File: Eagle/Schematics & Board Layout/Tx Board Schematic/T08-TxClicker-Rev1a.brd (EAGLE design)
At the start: 88.9 x 44.5 mm, 83 parts, among them U1 CC430F513X---RGZ48, X1-DNI SMA-SMD, Y1 26MHz

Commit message: layout update
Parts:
- added R17: (no value), QuadResistor:2012(4_RES)
- moved TP14 26.1 mm to (-18.5, 14.7)
- moved TP15 26.1 mm to (-18.5, 12.2)
- moved TP16 26.1 mm to (-18.5, 9.63)
- moved TP17 26.1 mm to (-18.5, 7.09)
- moved TP1 26.1 mm to (-20.4, 10.1)
- moved TP18 26.1 mm to (-16.0, 5.44)
- moved TP3 26.1 mm to (-23.0, 10.1)
- moved TP2 15.0 mm to (-12.7, 13.1)
- moved TP5 4.53 mm to (37.6, 22.7)
- moved C16 4.17 mm to (36.6, 7.72)
- moved C20 4.17 mm to (50.6, 2.13)
- moved C23 4.17 mm to (50.6, 4.67)
- moved C29 4.17 mm to (60.7, 9.88)
- moved C5 4.17 mm to (49.8, 24.6)
- moved C6 4.17 mm to (35.1, 24.7)
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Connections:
- new net N$19: R17.6, U1.2
- new net N$20: R17.8, U1.1
- new net N$7: R17.2, U1.4
- new net N$9: R17.4, U1.3
- net P1.7: now also R17.1; no longer U1.4
- net P2.0: now also R17.3; no longer U1.3
- net P2.1: now also R17.5; no longer U1.2
- net P2.2: now also R17.7; no longer U1.1
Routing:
- net P1.4: track 21.6 -> 41.3 mm, vias 2 -> 3
- net N$7: track 0.00 -> 7.17 mm
- net P2.1: track 19.6 -> 12.9 mm
- net P2.2: track 29.9 -> 24.1 mm
- net P1.7: track 44.2 -> 38.6 mm
- net N$9: track 0.00 -> 5.46 mm
- net N$15: track 45.9 -> 51.1 mm, vias 2 -> 0
- net RST/SBWTDIO: track 12.2 -> 8.19 mm
- net N$19: track 0.00 -> 3.80 mm
- net P2.0: track 30.9 -> 27.2 mm, vias 2 -> 0
- net P1.6/TX: track 19.9 -> 23.0 mm
- net N$20: track 0.00 -> 2.16 mm
- net P1.5/RX: track 21.7 -> 23.2 mm
- net VCC: track 155.7 -> 157.2 mm
- net TEST/SBWTCK: track 33.5 -> 34.0 mm, vias 2 -> 0
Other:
- board size 88.9 x 44.5 mm -> 84 x 41.7 mm

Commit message: layout update
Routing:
- net N$15: track 51.1 -> 46.9 mm, vias 0 -> 2
- net VCC: track 157.2 -> 158.4 mm
- net TEST/SBWTCK: track 34.0 -> 33.3 mm
- net P1.4: track 41.3 -> 41.4 mm, vias 3 -> 4

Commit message: Button Example
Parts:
- S1, S2, S3, S4: value TOUCHPAD_SWITCH_COMBO -> SWITCH-MOMENTARY-212MM
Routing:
- net P2.2: track 24.1 -> 29.4 mm
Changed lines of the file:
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@@
 <attribute name="OC_FARNELL" value="unknown" x="57.5564" y="18.0086" size="1.778" layer="27" display="off"/>
 </element>
-<element name="S1" library="SparkFun-Electromechanical--edited" package="TACTILE-PTH-12MM" value="TOUCHPAD_SWITCH_COMBO" x="46.6344" y="33.5026" rot="R270"/>
-<element name="S2" library="SparkFun-Electromechanical--edited" package="TACTILE-PTH-12MM" value="TOUCHPAD_SWITCH_COMBO" x="33.2994" y="33.6296" rot="R270"/>
-<element name="S3" library="SparkFun-Electromechanical--edited" package="TACTILE-PTH-12MM" value="TOUCHPAD_SWITCH_COMBO" x="20.2184" y="33.6296" rot="R270"/>
-<element name="S4" library="SparkFun-Electromechanical--edited" package="TACTILE-PTH-12MM" value="TOUCHPAD_SWITCH_COMBO" x="7.0104" y="33.6296" rot="R270"/>
+<element name="S1" library="SparkFun-Electromechanical--edited" package="TACTILE-PTH-12MM" value="SWITCH-MOMENTARY-212MM" x="46.6344" y="33.5026" rot="R270">
+<attribute name="PROD_ID" value="SWCH-09185" x="46.6344" y="33.5026" size="1.778" layer="27" rot="R270" display="off"/>
+</element>
+<element name="S2" library="SparkFun-Electromechanical--edited" package="TACTILE-PTH-12MM" value="SWITCH-MOMENTARY-212MM" x="33.2994" y="33.6296" rot="R270">
+<attribute name="PROD_ID" value="SWCH-09185" x="33.2994" y="33.6296" size="1.778" layer="27" rot="R270" display="off"/>
+</element>
+<element name="S3" library="SparkFun-Electromechanical--edited" package="TACTILE-PTH-12MM" value="SWITCH-MOMENTARY-212MM" x="20.2184" y="33.6296" rot="R270">
+<attribute name="PROD_ID" value="SWCH-09185" x="20.2184" y="33.6296" size="1.778" layer="27" rot="R270" display="off"/>
+</element>
+<element name="S4" library="SparkFun-Electromechanical--edited" package="TACTILE-PTH-12MM" value="SWITCH-MOMENTARY-212MM" x="7.0104" y="33.6296" rot="R270">
+<attribute name="PROD_ID" value="SWCH-09185" x="7.0104" y="33.6296" size="1.778" layer="27" rot="R270" display="off"/>
+</element>
 <element name="R7" library="rcl-amber" package="R0603" value="0-DNI" x="59.5884" y="11.4046" rot="R90"/>
 <element name="U$1" library="tagConnect" package="TC2030-MCP" value="TC2030-MCP" x="21.9964" y="8.1026" rot="R90"/>
@@
 <wire x1="48.4124" y1="25.2876" x2="49.8094" y2="25.2876" width="0.254" layer="1"/>
 <wire x1="49.8094" y1="25.2876" x2="49.8094" y2="25.3126" width="0.254" layer="1"/>
-<wire x1="49.8094" y1="25.3126" x2="49.8094" y2="26.5776" width="0.254" layer="1"/>
-<wire x1="49.8094" y1="26.5776" x2="49.1344" y2="27.2526" width="0.254" layer="1"/>
 <wire x1="49.8094" y1="25.3126" x2="51.3334" y2="25.3126" width="0.254" layer="1"/>
 <contactref element="R17" pad="7"/>
@@
 <wire x1="48.895" y1="20.9804" x2="50.6222" y2="22.7076" width="0.254" layer="1"/>
 <wire x1="50.6222" y1="22.7076" x2="51.3334" y2="22.7076" width="0.254" layer="1"/>
+<wire x1="49.8094" y1="25.3126" x2="52.197" y2="25.3126" width="0.4064" layer="1"/>
+<wire x1="52.197" y1="25.3126" x2="52.197" y2="28.2448" width="0.4064" layer="1"/>
+<wire x1="49.8094" y1="26.5776" x2="49.8094" y2="25.3126" width="0.4064" layer="1"/>
+<wire x1="49.8094" y1="26.5776" x2="49.1344" y2="27.2526" width="0.4064" layer="1"/>
 </signal>
 <signal name="P1.7">

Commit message: Arranging silkscreen
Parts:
- removed TP17: TEST-POINT3, SparkFun-Passives:PAD.03X.03
- added TP19, TP20, TP21, TP22, TP23, TP27, TP28: TEST-POINT3, SparkFun-Passives:PAD.03X.03
- LED1: value Blue -> (none)
- LED2: value Green -> (none)
- LED3: value Red -> (none)
- LED4: value Yellow -> (none)
- S1, S2, S3, S4: value SWITCH-MOMENTARY-212MM -> TOUCHPAD_SWITCH_COMBOSWITC_TOUCHPAD; device SparkFun-Electromechanical--edited:TACTILE-PTH-12MM -> button_TestFootprint:TACTILE-PTH-12MM
- moved TP16 62.9 mm to (43.8, 1.40), turned to 270 degrees
- moved TP15 62.3 mm to (43.1, 2.92), turned to 270 degrees
- moved TP14 62.1 mm to (42.2, 1.40), turned to 270 degrees
- moved TP18 61.5 mm to (45.3, 1.40), turned to 270 degrees
- moved TP3 59.2 mm to (35.6, 1.40)
- moved TP1 55.6 mm to (34.4, 1.40)
- moved TP2 47.4 mm to (33.3, 1.40)
- moved TP13 21.9 mm to (40.5, 1.40), turned to 270 degrees
- moved TP10 6.43 mm to (38.2, 2.92), turned to 270 degrees
- moved TP11 3.24 mm to (38.7, 1.40), turned to 270 degrees
- moved TP9 1.41 mm to (41.4, 2.92), turned to 270 degrees
- moved TP12 1.17 mm to (39.9, 2.92), turned to 270 degrees
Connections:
- removed net P1.0: TP9.P$1, U1.13
- removed net P1.1: TP10.P$1
- removed net P1.2: TP11.P$1
- removed net P1.3: TP12.P$1
- removed net P2.3: U1.48
- removed net P2.4: U1.47
- removed net P2.5: U1.46
- removed net P2.6: U1.24
- removed net P2.7: U1.23
- removed net P3.0: U1.21
- removed net P3.1: U1.20
- removed net P3.6: U1.15
- removed net P3.7: U1.14
- removed net P5.1: U1.43
- new net N$21: TP9.P$1, U1.17
- new net N$22: TP10.P$1, U1.13
- new net N$23: TP11.P$1, U1.14
- new net N$24: TP12.P$1, U1.15
- new net N$25: TP13.P$1, U1.16
- new net N$26: TP14.P$1, U1.18
- new net N$27: TP15.P$1, U1.19
- new net N$28: TP16.P$1, U1.20
- new net N$30: TP18.P$1, U1.23
- new net N$31: TP19.P$1, U1.24
- new net N$35: TP27.P$1, U1.47
- new net N$36: TP28.P$1, U1.48
- net N$11: now also S1.P$1, S2.P$1, S3.P$1, S4.P$1
- net P1.4: no longer TP13.P$1
- net P1.7: now also S4.P$2
- net P2.0: now also S3.P$2
- net P2.1: now also S2.P$2
- net P2.2: now also S1.P$2
- net PJ.0/TDO: now also TP23.P$1
- net PJ.1/TDI/TCLK: now also TP22.P$1
- net PJ.2/TMS: now also TP21.P$1
- net PJ.3/TCK: now also TP20.P$1
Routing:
- net N$11: track 59.1 -> 74.6 mm
- net N$23: track 0.00 -> 5.91 mm
- net N$25: track 0.00 -> 5.55 mm
- net N$26: track 0.00 -> 5.28 mm
- net N$31: track 0.00 -> 5.25 mm
- net N$30: track 0.00 -> 5.22 mm
- net P2.0: track 27.2 -> 32.2 mm
- net N$28: track 0.00 -> 5.01 mm
- net N$22: track 0.00 -> 4.43 mm
- net P2.1: track 12.9 -> 17.2 mm
- net N$24: track 0.00 -> 4.12 mm
- net P1.7: track 38.6 -> 42.7 mm
- net N$21: track 0.00 -> 3.87 mm
- net N$27: track 0.00 -> 3.60 mm
- net P1.0: track 2.64 -> 0.00 mm
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
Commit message: More Silkscreen
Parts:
- moved TP4 0.76 mm to (51.3, 23.5)
- moved R4 0.25 mm to (21.7, 24.7)
- moved R2 0.25 mm to (48.2, 24.6)
- moved R6 0.13 mm to (51.8, 12.3)
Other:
- board text added: "A"
- board text added: "B"
- board text added: "C"
- board text added: "D"

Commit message: And looking decent 0.o
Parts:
- removed R17: (no value), QuadResistor:2012(4_RES)
- added D1: UCLAMP3304A, Semtech-TVS_Diode:SOT666
- added R13, R14, R15, R16: 1k, rcl-amber:R0603
- added TP17, TP24, TP25, TP26: TEST-POINT3, SparkFun-Passives:PAD.03X.03
- LED1: value (none) -> Blue
- LED2: value (none) -> Green
- LED3: value (none) -> Yellow
- LED4: value (none) -> Red
- moved TP1 44.6 mm to (59.1, 38.6)
- moved LED1 39.6 mm to (46.6, 24.6)
- moved LED4 39.6 mm to (7.01, 24.9)
- moved TP2 31.9 mm to (2.16, 8.38)
- moved TP3 24.1 mm to (59.7, 1.91)
- moved LED3 13.1 mm to (20.2, 24.7)
- moved LED2 13.0 mm to (33.3, 24.7)
- moved TP9 3.18 mm to (38.2, 2.92)
- moved TP11 1.91 mm to (39.9, 2.92)
- moved TP13 1.76 mm to (41.4, 2.92)
- moved TP12 1.65 mm to (40.5, 1.40)
- moved TP10 1.61 mm to (38.7, 1.40)
- moved C32 0.74 mm to (43.2, 16.5)
- moved C27 0.64 mm to (41.8, 16.5)
- moved R2 0.13 mm to (48.3, 24.6)
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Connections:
- removed net RST/SBWTDIO: C1.1, R12.1, U$1.4
- net GND: now also D1.2, D1.5
- net N$10: now also LED2.C; no longer LED3.C
- net N$13: now also LED4.A; no longer LED1.A
- net N$14: now also LED3.A; no longer LED2.A
- net N$15: now also LED3.C; no longer LED2.C
- net N$16: now also LED2.A; no longer LED3.A
- net N$17: now also LED1.A; no longer LED4.A
- net N$18: now also LED4.C; no longer LED1.C
- net N$19: now also R14.2; no longer R17.6
- net N$20: now also R13.2; no longer R17.8
- net N$21: now also TP13.P$1; no longer TP9.P$1
- net N$22: now also TP9.P$1; no longer TP10.P$1
- net N$23: now also TP10.P$1; no longer TP11.P$1
- net N$24: now also TP11.P$1; no longer TP12.P$1
- net N$25: now also TP12.P$1; no longer TP13.P$1
- net N$7: now also R16.2; no longer R17.2
- net N$9: now also R15.2; no longer R17.4
- net P1.4: now also LED1.C; no longer LED4.C
- net P1.5/RX: now also TP26.P$1
- net P1.6/TX: now also TP17.P$1
- net P1.7: now also D1.4, R16.1; no longer R17.1
- net P2.0: now also D1.6, R15.1; no longer R17.3
- net P2.1: now also D1.1, R14.1; no longer R17.5
- net P2.2: now also D1.3, R13.1; no longer R17.7
- net RST/NMI/SBWTDIO: now also C1.1, R12.1, TP24.P$1, U$1.4
- net TEST/SBWTCK: now also TP25.P$1
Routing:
- net RST/NMI/SBWTDIO: track 0.00 -> 41.7 mm, vias 0 -> 2
- net P1.7: track 42.7 -> 76.5 mm, vias 2 -> 4
- net P2.0: track 32.5 -> 47.8 mm, vias 0 -> 2
- net RST/SBWTDIO: track 8.19 -> 0.00 mm
- net N$11: track 74.6 -> 67.1 mm
- net P2.1: track 17.2 -> 20.0 mm
- net GND: track 5.42 -> 7.56 mm, vias 2 -> 13
- net P1.5/RX: track 23.2 -> 24.2 mm
- net P2.2: track 29.3 -> 30.1 mm
- net P1.4: track 40.9 -> 40.2 mm
- net TEST/SBWTCK: track 33.3 -> 33.9 mm, vias 0 -> 2
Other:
- board size 84 x 41.7 mm -> 83.8 x 42.2 mm
- board text added: "Portland State University Team: T08 Nov2014"
- board text removed: "Portland State University Team: T08"

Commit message: fill and crystal tweak
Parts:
- moved C20 0.25 mm to (50.6, 2.39)
- moved Y1 0.25 mm to (48.4, 3.66)
- moved C23 0.25 mm to (50.6, 4.93)
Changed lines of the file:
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@@
 <attribute name="VALUE" x="44.7294" y="25.2476" size="1.27" layer="27" rot="R270"/>
 </element>
-<element name="C23" library="rcl-amber" package="C0603" value="18pF" x="50.5714" y="4.6736" smashed="yes" rot="R270">
-<attribute name="NAME" x="51.562" y="4.064" size="0.508" layer="25" rot="R90"/>
-<attribute name="VALUE" x="52.324" y="4.064" size="0.508" layer="27" rot="R90"/>
-</element>
-<element name="C20" library="rcl-amber" package="C0603" value="18pF" x="50.5714" y="2.1336" smashed="yes" rot="R90">
-<attribute name="NAME" x="51.6314" y="1.4276" size="0.508" layer="25" rot="R90"/>
-<attribute name="VALUE" x="52.3304" y="1.4276" size="0.508" layer="27" rot="R90"/>
+<element name="C23" library="rcl-amber" package="C0603" value="18pF" x="50.5714" y="4.9276" smashed="yes" rot="R270">
+<attribute name="NAME" x="51.562" y="4.318" size="0.508" layer="25" rot="R90"/>
+<attribute name="VALUE" x="52.324" y="4.318" size="0.508" layer="27" rot="R90"/>
+</element>
+<element name="C20" library="rcl-amber" package="C0603" value="18pF" x="50.5714" y="2.3876" smashed="yes" rot="R90">
+<attribute name="NAME" x="51.6314" y="1.6816" size="0.508" layer="25" rot="R90"/>
+<attribute name="VALUE" x="52.3304" y="1.6816" size="0.508" layer="27" rot="R90"/>
 </element>
 <element name="C5" library="rcl-amber" package="C0603" value="DNI" x="49.8094" y="24.6126" smashed="yes" rot="R270">
@@
 <attribute name="VALUE" x="60.6964" y="8.0106" size="0.254" layer="27" rot="R90"/>
 </element>
-<element name="Y1" library="SparkFun-FreqCtrl" package="CRYSTAL-TXC-7A" value="26MHz" x="48.4124" y="3.4036" smashed="yes" rot="R270">
-<attribute name="NAME" x="46.2534" y="5.8166" size="0.508" layer="25" rot="R270"/>
-<attribute name="VALUE" x="46.1264" y="4.8006" size="0.508" layer="27" rot="R270"/>
+<element name="Y1" library="SparkFun-FreqCtrl" package="CRYSTAL-TXC-7A" value="26MHz" x="48.4124" y="3.6576" smashed="yes" rot="R270">
+<attribute name="NAME" x="46.2534" y="6.0706" size="0.508" layer="25" rot="R270"/>
+<attribute name="VALUE" x="46.1264" y="5.0546" size="0.508" layer="27" rot="R270"/>
 </element>
 <element name="TP4" library="SparkFun-Passives" package="PAD.03X.03" value="TEST-POINT3" x="51.3334" y="23.4696" smashed="yes" rot="R270"/>
@@
 <polygon width="0.254" layer="16">
 <vertex x="0" y="0"/>
-<vertex x="61.8236" y="0.1016"/>
-<vertex x="61.8236" y="41.7322"/>
-<vertex x="0" y="41.6306"/>
+<vertex x="61.8236" y="0"/>
+<vertex x="61.8236" y="42.164"/>
+<vertex x="0" y="42.164"/>
 </polygon>
 <contactref element="X1-DNI" pad="2@2"/>
@@
 <polygon width="0.254" layer="1" isolate="0.254">
 <vertex x="0" y="0"/>
-<vertex x="61.8236" y="0.1016"/>
-<vertex x="61.8236" y="41.7322"/>
-<vertex x="0" y="41.6306"/>
+<vertex x="61.8236" y="0"/>
+<vertex x="61.8236" y="42.164"/>
+<vertex x="0" y="42.164"/>
 </polygon>
 <wire x1="43.3284" y1="13.6116" x2="43.3284" y2="9.1146" width="0.254" layer="1"/>
@@
 <wire x1="43.3284" y1="9.1146" x2="44.9834" y2="8.1026" width="0" layer="19" extent="1-1"/>
 <wire x1="36.6014" y1="24.0646" x2="37.9984" y2="21.0566" width="0" layer="19" extent="1-1"/>
-<wire x1="54.5004" y1="7.7216" x2="52.4684" y2="10.6426" width="0" layer="19" extent="1-1"/>
 <wire x1="43.2054" y1="17.1846" x2="43.3284" y2="13.6116" width="0" layer="19" extent="1-1"/>
 <wire x1="33.3614" y1="9.7536" x2="31.3944" y2="13.9446" width="0" layer="19" extent="1-1"/>
@@
 <contactref element="C20" pad="1"/>
 <contactref element="Y1" pad="P$1"/>
-<wire x1="46.6824" y1="7.2576" x2="46.6824" y2="2.0856" width="0.254" layer="1"/>
-<wire x1="46.6824" y1="2.0856" x2="47.8804" y2="2.0856" width="0.254" layer="1"/>
-<wire x1="47.8804" y1="2.0856" x2="48.4124" y2="1.5536" width="0.4064" layer="1"/>
-<wire x1="50.5714" y1="1.4336" x2="48.5324" y2="1.4336" width="0.4064" layer="1"/>
-<wire x1="48.5324" y1="1.4336" x2="48.4124" y2="1.5536" width="0.254" layer="1"/>
+<wire x1="46.6824" y1="7.2576" x2="46.6824" y2="2.3396" width="0.254" layer="1"/>
+<wire x1="46.6824" y1="2.3396" x2="47.8804" y2="2.3396" width="0.254" layer="1"/>
+<wire x1="47.8804" y1="2.3396" x2="48.4124" y2="1.8076" width="0.4064" layer="1"/>
+<wire x1="50.5714" y1="1.6876" x2="48.5324" y2="1.6876" width="0.4064" layer="1"/>
+<wire x1="48.5324" y1="1.6876" x2="48.4124" y2="1.8076" width="0.254" layer="1"/>
 </signal>
 <signal name="RF_XOUT">
@@
 <contactref element="C23" pad="1"/>
 <contactref element="Y1" pad="P$2"/>
-<wire x1="48.6594" y1="5.5006" x2="48.4124" y2="5.2536" width="0.254" layer="1"/>
-<wire x1="50.5714" y1="5.3736" x2="50.5714" y2="5.3086" width="0.254" layer="1"/>
+<wire x1="48.6594" y1="5.7546" x2="48.4124" y2="5.5076" width="0.254" layer="1"/>
+<wire x1="50.5714" y1="5.6276" x2="50.5714" y2="5.5626" width="0.254" layer="1"/>
 <wire x1="46.6824" y1="7.7576" x2="46.3804" y2="7.7576" width="0.254" layer="1"/>
 <wire x1="46.6824" y1="7.7576" x2="47.4874" y2="7.7576" width="0.254" layer="1"/>
 <wire x1="47.4874" y1="7.7576" x2="48.5394" y2="6.7056" width="0.254" layer="1"/>
-<wire x1="48.5394" y1="6.7056" x2="48.5394" y2="5.3806" width="0.254" layer="1"/>
-<wire x1="48.5394" y1="5.3806" x2="48.4124" y2="5.2536" width="0.254" layer="1"/>
-<wire x1="50.5714" y1="5.3086" x2="48.4674" y2="5.3086" width="0.4064" layer="1"/>
-<wire x1="48.4674" y1="5.3086" x2="48.4124" y2="5.2536" width="0.4064" layer="1"/>
+<wire x1="48.5394" y1="6.7056" x2="48.5394" y2="5.6346" width="0.254" layer="1"/>
+<wire x1="48.5394" y1="5.6346" x2="48.4124" y2="5.5076" width="0.254" layer="1"/>
+<wire x1="50.5714" y1="5.5626" x2="48.4674" y2="5.5626" width="0.4064" layer="1"/>
+<wire x1="48.4674" y1="5.5626" x2="48.4124" y2="5.5076" width="0.4064" layer="1"/>
 </signal>
 <signal name="RF_P">

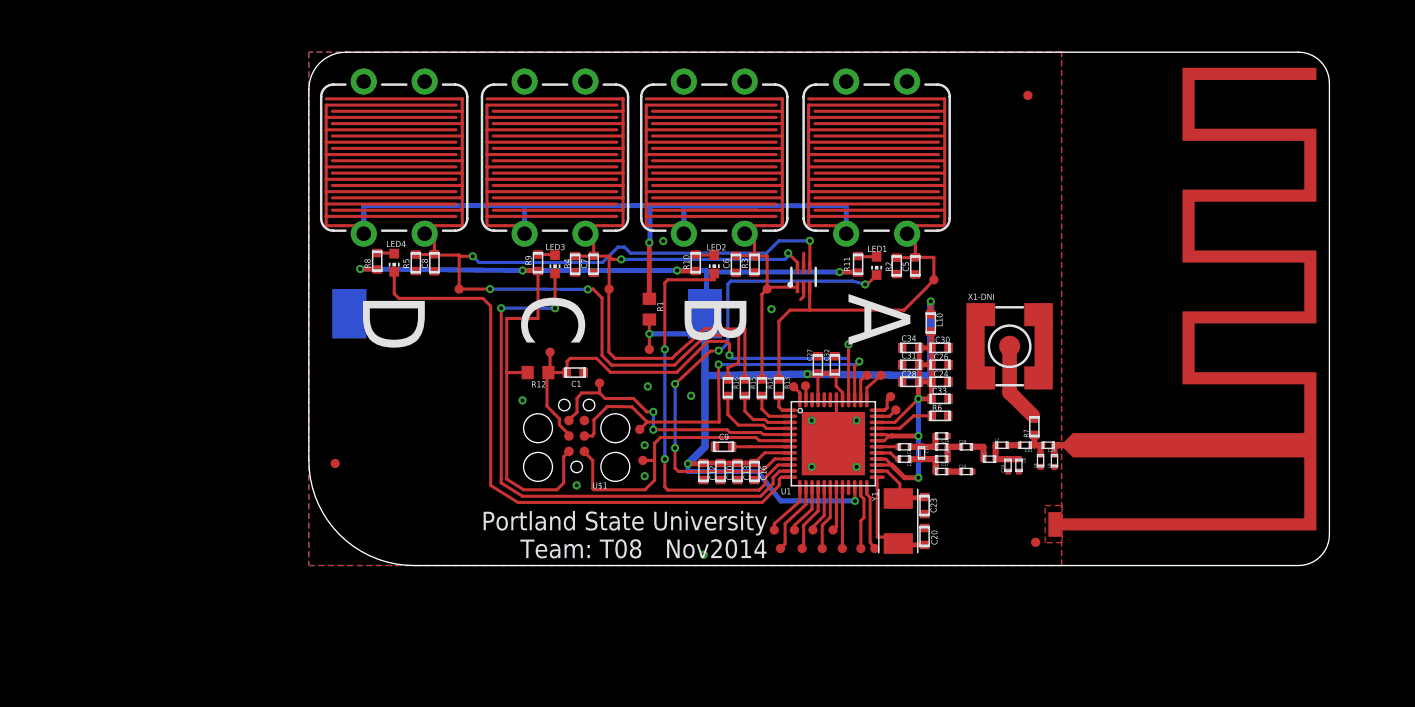
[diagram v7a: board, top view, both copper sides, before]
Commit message: Move Tag Connect
Vectorized fonts, moved tag connect, added tp labels
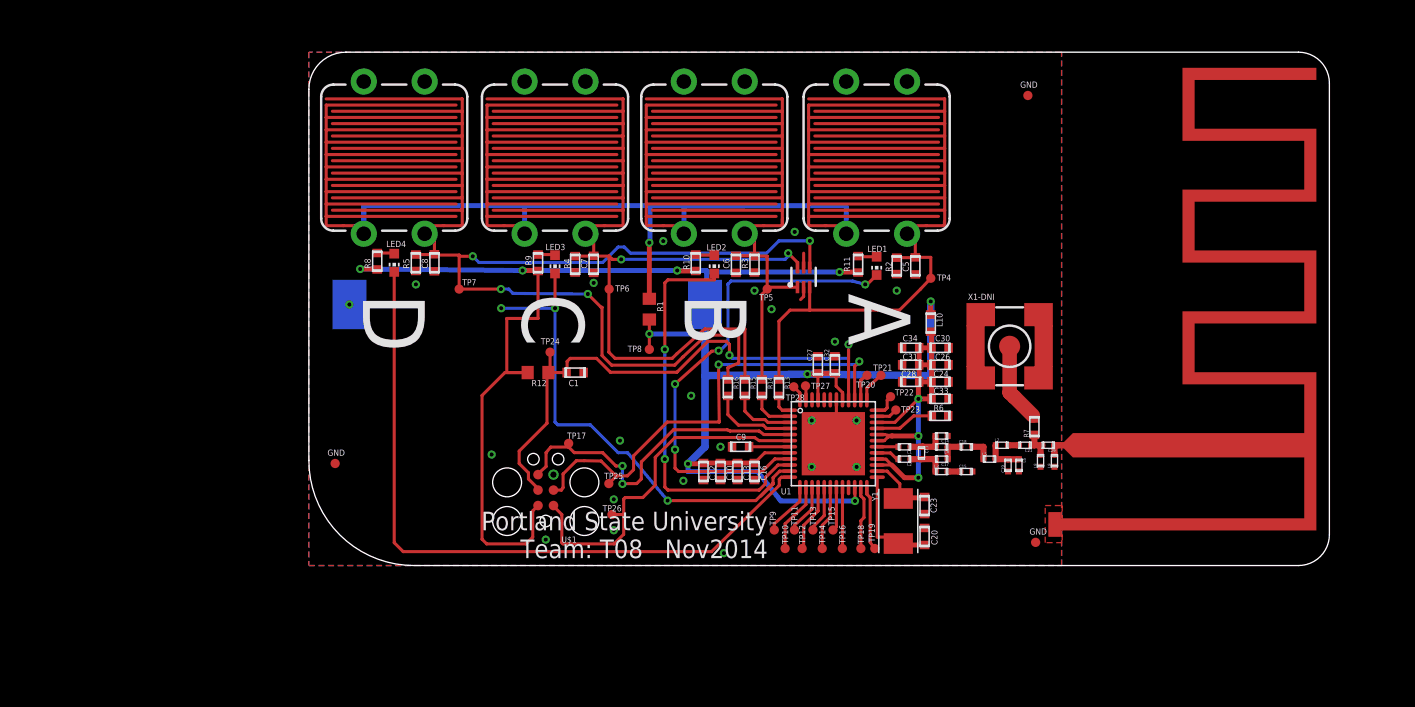
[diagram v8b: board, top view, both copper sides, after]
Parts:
- TP1, TP10, TP11, TP12, TP13, TP14, TP15, TP16, TP17, TP18, TP19, TP2, TP20, TP21, TP22, TP23, TP24, TP25, TP26, TP27, TP28, TP3, TP5, TP6, TP7, TP8: value TEST-POINT3 -> (none)
- TP9: value TEST-POINT3 -> TP9
- moved TP17 5.57 mm to (21.3, 10.0)
- moved U$1 5.12 mm to (19.5, 3.66)
- moved TP25 5.12 mm to (24.6, 6.73)
- moved TP26 5.12 mm to (24.9, 4.19)
- moved C9 1.40 mm to (35.5, 9.75)
- moved U$5 0.76 mm to (17.9, 21.4)
- moved TP10 0.38 mm to (39.1, 1.40)
- moved TP4 0.28 mm to (51.1, 23.6)
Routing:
- net VCC: track 158.2 -> 165.5 mm
- net N$18: track 51.0 -> 57.8 mm
- net P1.5/RX: track 24.2 -> 29.8 mm
- net RST/NMI/SBWTDIO: track 41.7 -> 47.0 mm
- net N$15: track 46.8 -> 41.5 mm, vias 2 -> 3
- net TEST/SBWTCK: track 33.9 -> 38.9 mm
- net P1.6/TX: track 22.8 -> 27.5 mm
- net GND: track 7.56 -> 9.81 mm, vias 13 -> 23
- net VCORE: track 4.71 -> 3.32 mm
- net P2.2: track 30.1 -> 29.6 mm
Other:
- board text added: "GND"
- board text removed: "1"
- board text removed: "12"
- board text removed: "24"
- board text removed: "36"
